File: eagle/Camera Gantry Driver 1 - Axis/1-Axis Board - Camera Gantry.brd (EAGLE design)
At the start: 72.5 x 47.3 mm, 47 parts, among them IC1 DRV8312A, U1 PTN78000, U2 DSPIC33FJ802GP-28, U3 LP2950-3.3ACZ

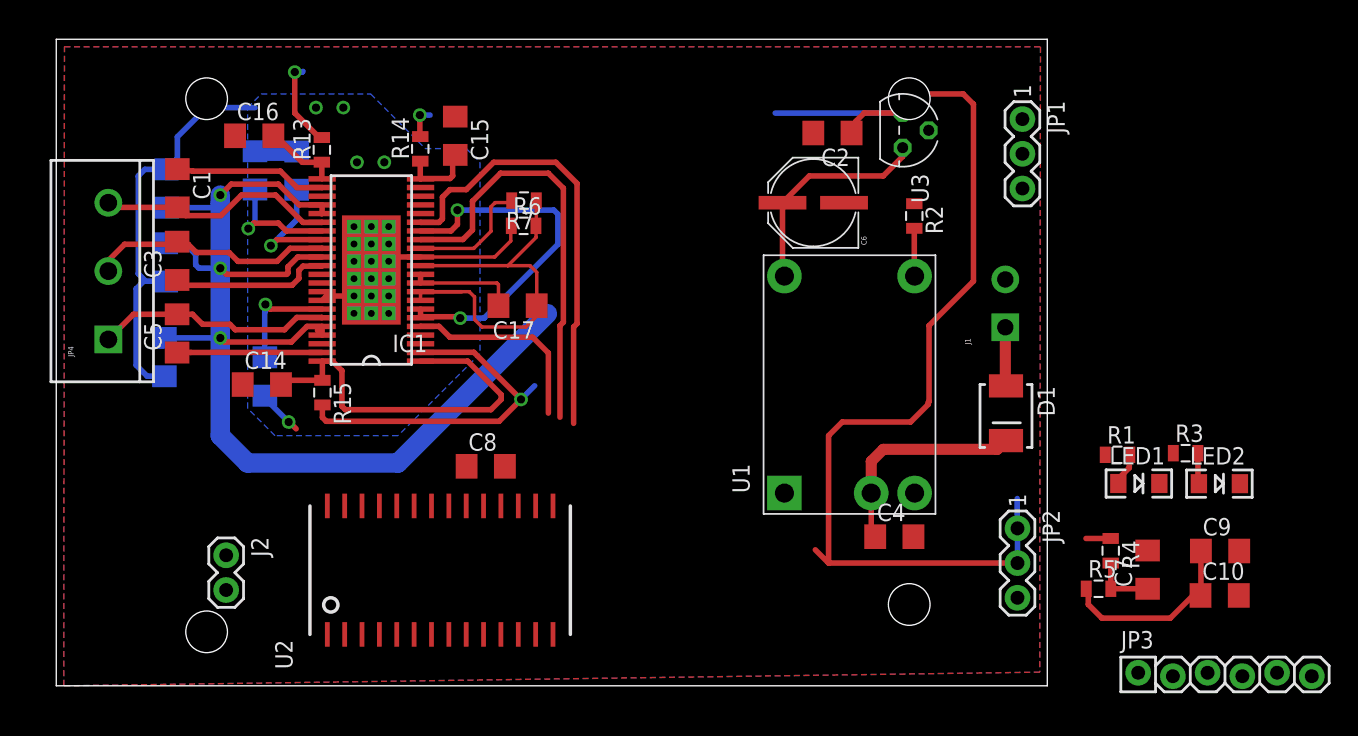
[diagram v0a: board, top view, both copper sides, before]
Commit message: Finished 1-Axis Dev for Camera Stab.
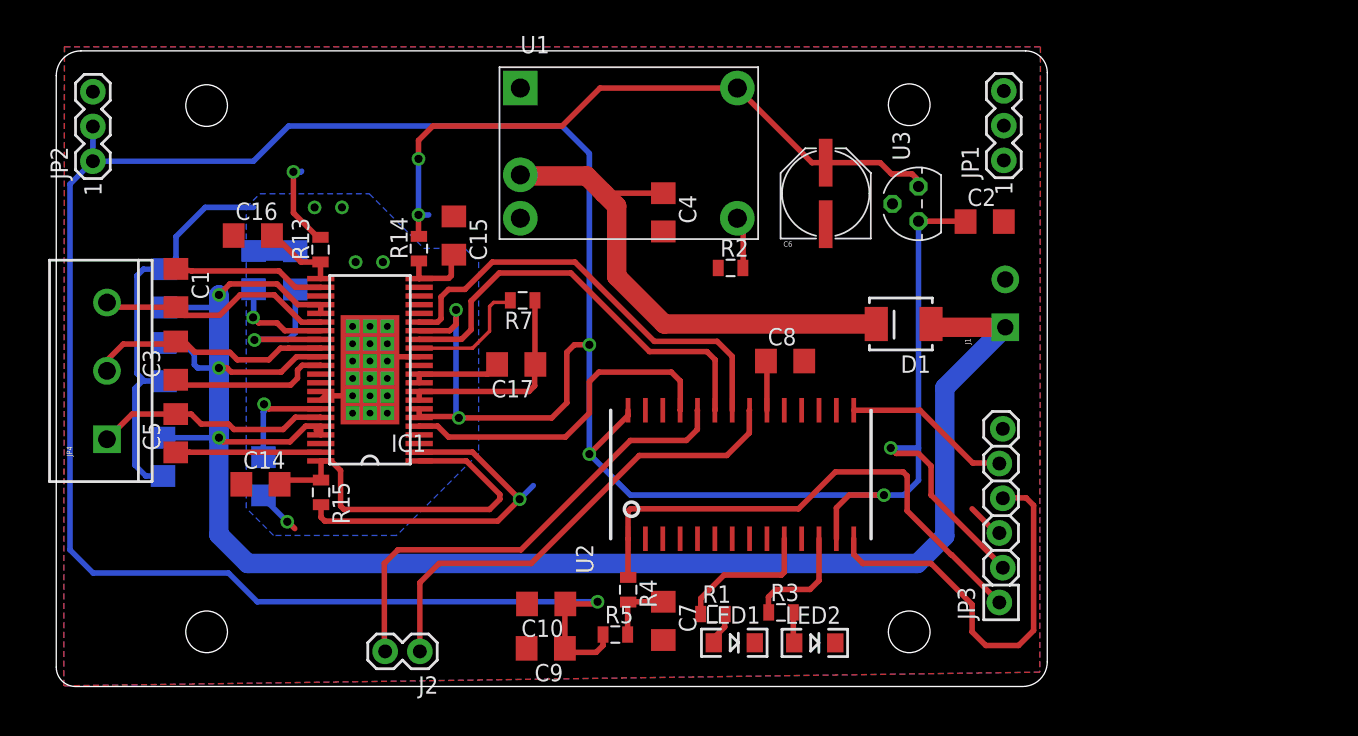
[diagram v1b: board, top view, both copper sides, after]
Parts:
- removed R6: 1 Ohm, ASL:0805
- moved JP2 74.8 mm to (2.68, 41.0), turned to 90 degrees
- moved C9 49.8 mm to (35.8, 2.79), turned to 180 degrees
- moved C10 49.3 mm to (35.8, 6.04), turned to 180 degrees
- moved C7 35.6 mm to (44.4, 4.80), turned to 270 degrees
- moved R5 35.5 mm to (40.9, 3.80)
- moved R4 35.4 mm to (41.8, 7.08)
- moved U1 35.4 mm to (34.0, 43.8), turned to 0 degrees
- moved LED1 31.8 mm to (49.6, 3.20)
- moved LED2 31.8 mm to (55.5, 3.19)
- moved R1 31.8 mm to (48.0, 5.30)
- moved R3 31.8 mm to (53.0, 5.42)
- moved C4 29.1 mm to (44.4, 34.7), turned to 270 degrees
- moved C8 23.2 mm to (53.3, 23.8)
- moved U2 23.1 mm to (50.2, 15.4)
- moved J2 15.8 mm to (26.6, 2.57), turned to 180 degrees
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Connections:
- net AGND: no longer IC1.12, R6.2
- net GND: now also IC1.12; no longer R6.1
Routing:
- net VCC3V3: track 121.9 -> 244.9 mm, vias 2 -> 7
- net PVDD: track 91.2 -> 145.3 mm
- net MCLR: track 1.81 -> 38.7 mm
- net UART_TX: track 0.00 -> 35.3 mm
- net UART_RX: track 0.00 -> 34.8 mm
- net VCC: track 51.5 -> 82.1 mm, vias 3 -> 4
- net PGD: track 0.00 -> 30.3 mm
- net N$8: track 16.1 -> 37.9 mm
- net AGND: track 32.9 -> 18.6 mm
- net PGC: track 0.00 -> 12.3 mm
- net PWM1: track 14.6 -> 25.2 mm
- net LED1: track 0.00 -> 10.5 mm
- net LED2: track 0.00 -> 8.40 mm
- net GND: track 50.1 -> 44.6 mm
- net N$7: track 0.00 -> 3.63 mm
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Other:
- board size 72.5 x 47.3 mm -> 72.5 x 46.5 mm

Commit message: Added some filtering to the 1-Axis Gantry Board
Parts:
- removed R11, R12: 1mOhm, ASL:1206
- removed R13, R14, R15: 5, ASL:0805
- added C18: 1000uF, ASL:CPOL-RADIAL-1000UF-25V
- added C19: 10nF, ASL:1206
- added C20, C21: 220uF, ASL:CPOL-RADIAL-100UF-25V
- added R6, R8, R9: (no value), pavlo:SMT-REF
- C14, C15, C16: value 1uF -> 220nF
- C6: device CMPE118lib:CPOL_6.6 -> ASL:CPOL-RADIAL-100UF-25V
- R10: value 1mOhm -> 3.3Ohm; device ASL:1206 -> ASL:0805
- moved R10 25.8 mm to (17.5, 41.0), flipped to the top
- moved C15 9.84 mm to (28.5, 42.8), turned to 0 degrees
- moved JP4 1.52 mm to (2.19, 18.1)
- moved C6 1.37 mm to (55.4, 37.1), turned to 270 degrees
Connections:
- removed net N$14: C15.2, IC1.22, R14.1
- removed net N$16: C14.2, IC1.1, IC1.44, R15.1
- net GND: now also C18.2, C19.2, C20.2, C21.2, C6.2, R6.2, R8.2, R9.2; no longer C6.-, R10.2, R11.2, R12.2
- net N$11: now also R8.1; no longer R11.1
- net N$12: now also IC1.38, R9.1; no longer IC1.29, R12.1
- net N$13: now also C19.1, R10.1; no longer C16.2, IC1.23, R13.1
- net N$9: now also IC1.29, R6.1; no longer IC1.38, R10.1
- net PVDD: now also C18.1, R10.2
- net VCC: now also C14.2, C15.2, C16.2, C20.1, C21.1, C6.1, IC1.1, IC1.22, IC1.23, IC1.44; no longer C6.+, R13.2, R14.2, R15.2
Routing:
- net N$16: track 28.3 -> 0.00 mm
- net VCC: track 82.1 -> 103.1 mm, vias 4 -> 2
- net PVDD: track 145.3 -> 165.4 mm
- net N$12: track 7.43 -> 21.8 mm
- net N$14: track 5.36 -> 0.00 mm
- net N$13: track 5.59 -> 2.76 mm
- net N$9: track 8.18 -> 10.4 mm
- net N$11: track 11.2 -> 9.39 mm
- net GND: track 44.6 -> 46.3 mm, vias 5 -> 3
- net N$10: track 17.3 -> 18.8 mm
- net N$4: track 17.5 -> 19.0 mm
- net N$5: track 18.6 -> 19.6 mm
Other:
- board size 72.5 x 46.5 mm -> 73.3 x 46.5 mm
